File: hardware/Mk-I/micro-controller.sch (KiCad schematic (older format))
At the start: 31 parts, among them U10 STM32_SWD_Connector, U4 STM32F407VG, U8 MOLEX_microSD_47219-2001, X1 CRYSTAL

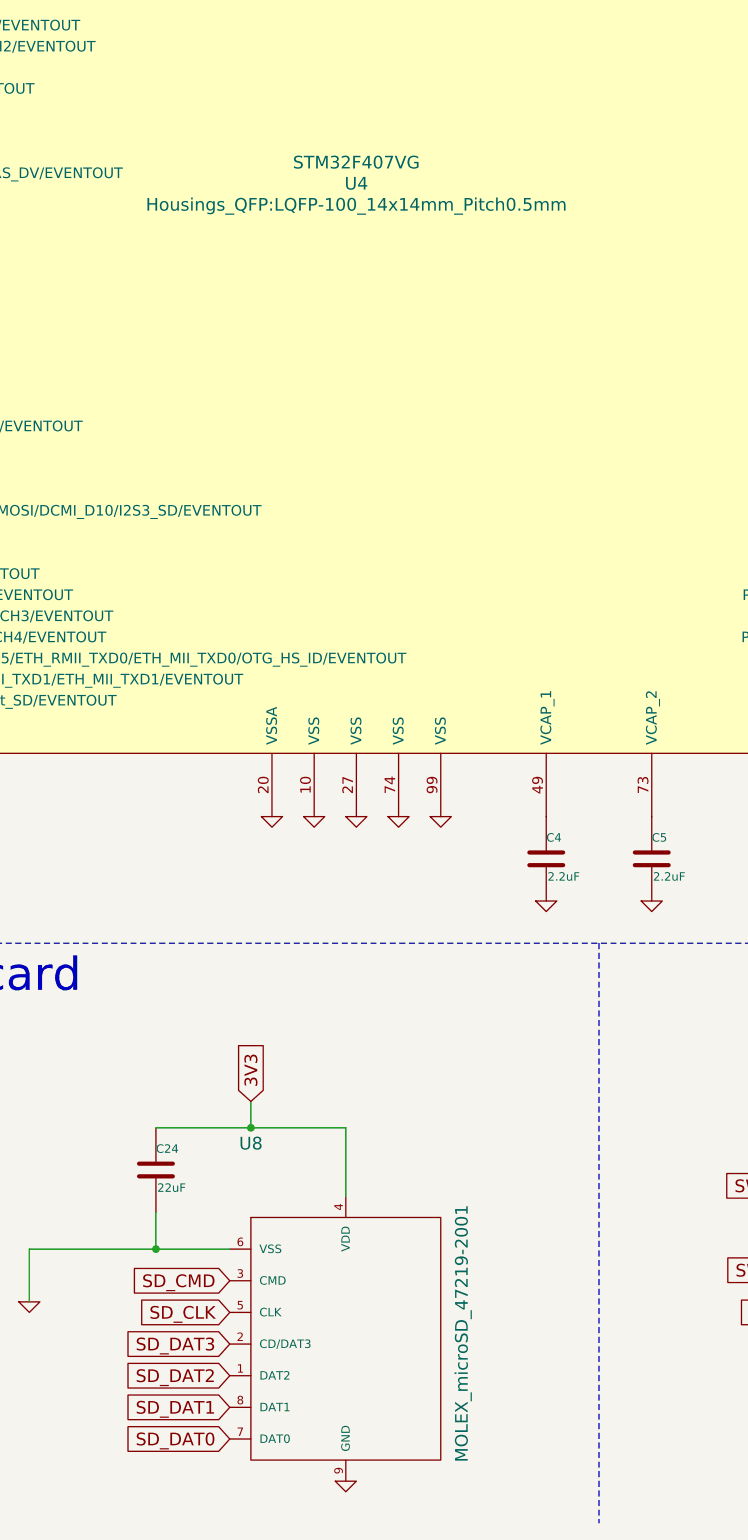
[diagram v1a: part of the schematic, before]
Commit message: HW: Update parts value
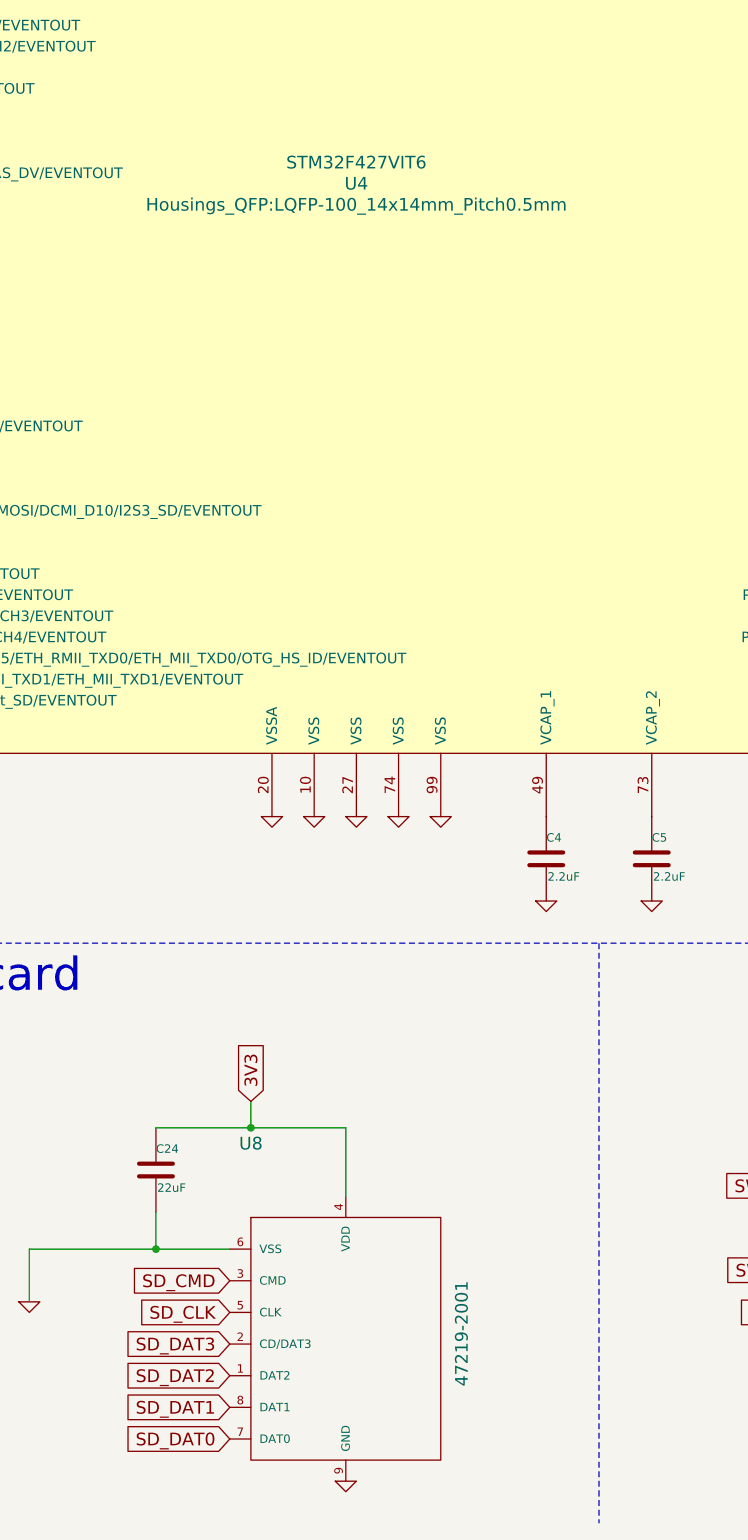
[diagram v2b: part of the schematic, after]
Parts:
- U4: value STM32F407VG -> STM32F427VIT6
- U8: value MOLEX_microSD_47219-2001 -> 47219-2001
- X1: value CRYSTAL -> AS-8.000-18
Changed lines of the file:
@@
 P 2300 3000
 F 0 "X1" H 2300 3150 60  0000 C CNN
-F 1 "CRYSTAL" H 2300 2850 60  0000 C CNN
+F 1 "AS-8.000-18" H 2300 2850 60  0000 C CNN
 F 2 "Crystals:Crystal_HC49-U_Vertical" H 2300 3000 60  0001 C CNN
 F 3 "" H 2300 3000 60  0000 C CNN
@@
 P 7850 4850
 F 0 "U4" H 7850 4850 60  0000 C CNN
-F 1 "STM32F407VG" H 7850 4950 60  0000 C CNN
+F 1 "STM32F427VIT6" H 7850 4950 60  0000 C CNN
 F 2 "Housings_QFP:LQFP-100_14x14mm_Pitch0.5mm" H 7850 4750 60  0000 C CNN
 F 3 "" H 7850 4850 60  0001 C CNN
@@
 P 7350 9400
 F 0 "U8" H 7350 9400 60  0000 C CNN
-F 1 "MOLEX_microSD_47219-2001" V 8350 8500 60  0000 C CNN
+F 1 "47219-2001" V 8350 8500 60  0000 C CNN
 F 2 "POSS:MOLEX_microSD_47219-2001" H 7350 9400 60  0001 C CNN
 F 3 "" H 7350 9400 60  0001 C CNN

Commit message: HW: Change crystal for a smd package
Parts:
- removed X1: AS-8.000-18, Crystals:Crystal_HC49-U_Vertical, symbol CRYSTAL
- added X1: ABM3B-8.000MHZ-B2-T, Crystals:Crystal_SMD_0603_4Pads, symbol Crystal_GND24
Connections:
- wire segments 46 -> 52
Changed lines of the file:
@@
 WAKEUP
-$Comp
-L CRYSTAL X1
-U 1 1 585F8666
-P 2300 3000
-F 0 "X1" H 2300 3150 60  0000 C CNN
-F 1 "AS-8.000-18" H 2300 2850 60  0000 C CNN
-F 2 "Crystals:Crystal_HC49-U_Vertical" H 2300 3000 60  0001 C CNN
-F 3 "" H 2300 3000 60  0000 C CNN
-	1    2300 3000
-	0    1    1    0
-$EndComp
 $Comp
 L C-RESCUE-wnm_mk_1 C12
@@
 Wire Wire Line
 	2600 9900 1900 9900
+$Comp
+L Crystal_GND24 X1
+U 1 1 59EB52C9
+P 2300 3000
+F 0 "X1" V 2100 3100 50  0000 L CNN
+F 1 "ABM3B-8.000MHZ-B2-T" V 1900 2350 50  0000 L CNN
+F 2 "Crystals:Crystal_SMD_0603_4Pads" H 2300 3000 50  0001 C CNN
+F 3 "" H 2300 3000 50  0001 C CNN
+	1    2300 3000
+	0    -1   -1   0
+$EndComp
+Wire Wire Line
+	2300 2700 2300 2850
+Wire Wire Line
+	2300 3150 2300 3300
+Wire Wire Line
+	2500 3000 2550 3000
+Wire Wire Line
+	2550 3000 2550 3050
+Wire Wire Line
+	2100 3000 2050 3000
+Wire Wire Line
+	2050 3000 2050 3050
+$Comp
+L GND-RESCUE-wnm_mk_1 #PWR032
+U 1 1 59EB6029
+P 2050 3050
+F 0 "#PWR032" H 2050 3050 30  0001 C CNN
+F 1 "GND" H 2050 2980 30  0001 C CNN
+F 2 "" H 2050 3050 60  0001 C CNN
+F 3 "" H 2050 3050 60  0001 C CNN
+	1    2050 3050
+	1    0    0    -1
+$EndComp
+$Comp
+L GND-RESCUE-wnm_mk_1 #PWR033
+U 1 1 59EB60D4
+P 2550 3050
+F 0 "#PWR033" H 2550 3050 30  0001 C CNN
+F 1 "GND" H 2550 2980 30  0001 C CNN
+F 2 "" H 2550 3050 60  0001 C CNN
+F 3 "" H 2550 3050 60  0001 C CNN
+	1    2550 3050
+	1    0    0    -1
+$EndComp
 $EndSCHEMATC

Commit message: HW: Major change of layout...
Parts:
- removed ext1: CONN_01X04, Socket_Strips:Socket_Strip_Straight_1x04, symbol CONN_01X04
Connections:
- net labels added: PLAY_WAKEUP
- net labels removed: B1, B11, B12, B13, B14, B15, B16, B2, B3, B4, B5, B6, B7, B8, B9, BA, BB, BC, BD, BE, FX, Play, ROW3, WAKEUP
- wire segments 52 -> 51
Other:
- moved on the sheet: R3, R4

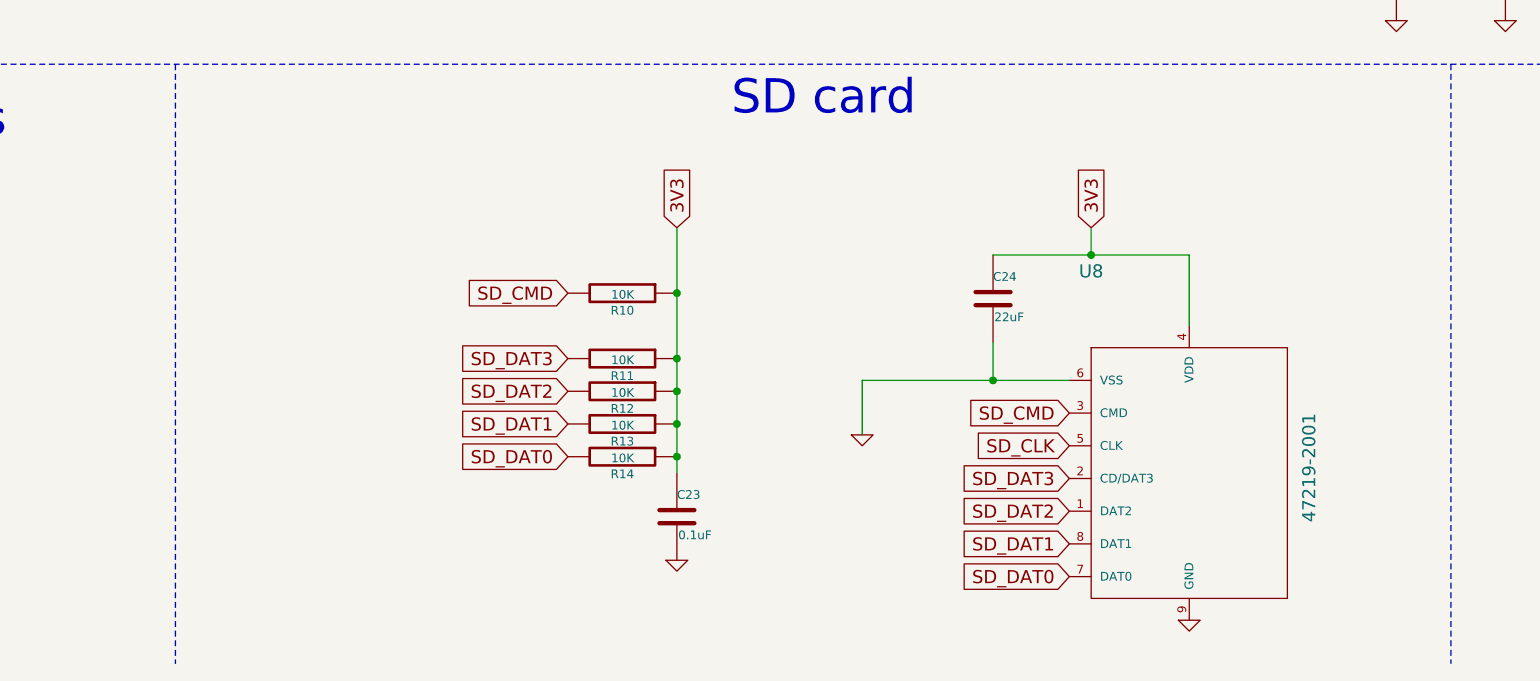
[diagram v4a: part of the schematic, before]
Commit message: HW: Change micro SD card slot
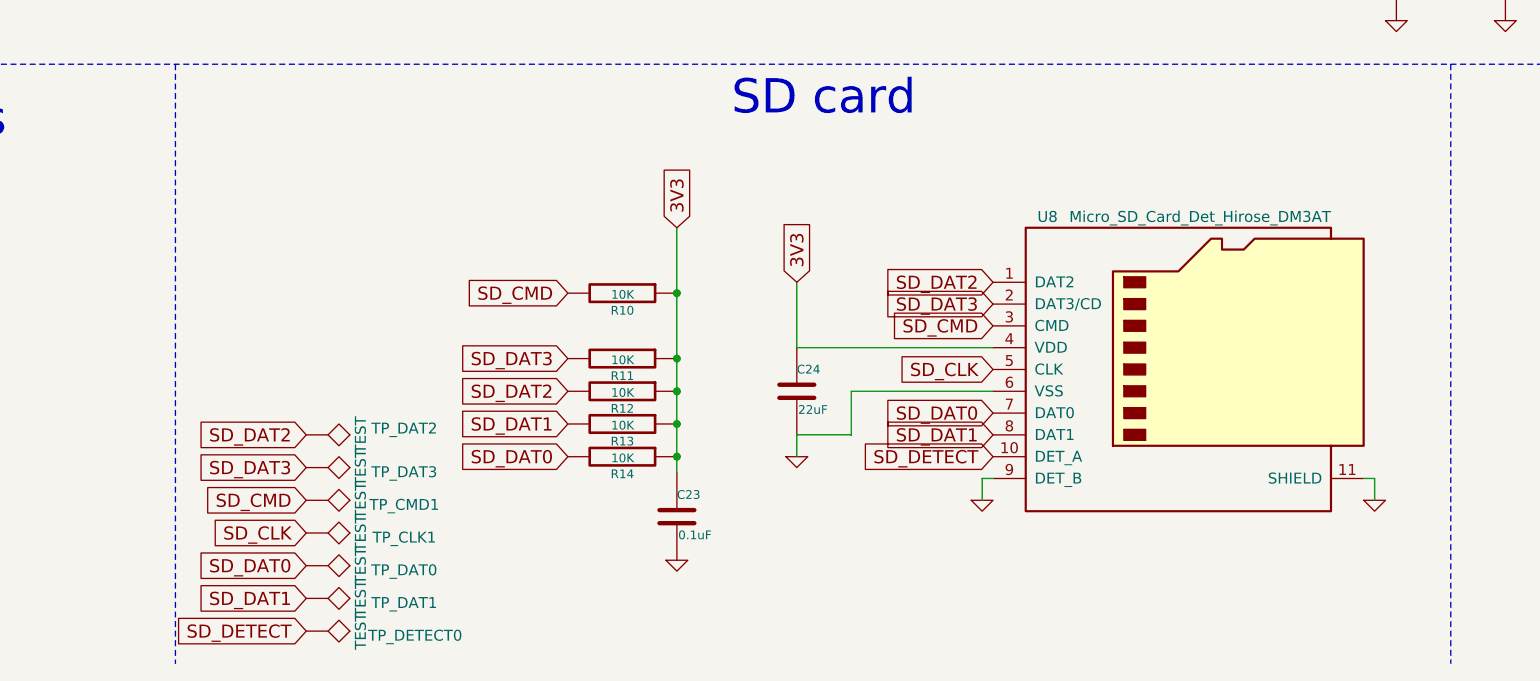
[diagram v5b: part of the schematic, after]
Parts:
- removed U8: 47219-2001, POSS:MOLEX_microSD_47219-2001, symbol MOLEX_microSD_47219-2001
- added TP_CLK1, TP_CMD1, TP_DAT0, TP_DAT1, TP_DAT2, TP_DAT3, TP_DETECT0: TEST, Measurement_Points:Measurement_Point_Round-SMD-Pad_Small, symbol TEST
- added U8: Micro_SD_Card_Det_Hirose_DM3AT, POSS:DM3D, symbol Micro_SD_Card_Det_Hirose_DM3AT
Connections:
- net 3V3: now also U8.4 (VDD)
- net GND: now also U8.11 (SHIELD), U8.6 (VSS), U8.9 (DET_B)
- net SD_CLK: now also TP_CLK1.1, U8.5 (CLK)
- net SD_CMD: now also TP_CMD1.1, U8.3 (CMD)
- net SD_DAT0: now also TP_DAT0.1, U8.7 (DAT0)
- net SD_DAT1: now also TP_DAT1.1, U8.8 (DAT1)
- net SD_DAT2: now also TP_DAT2.1, U8.1 (DAT2)
- net SD_DAT3: now also TP_DAT3.1, U8.2 (DAT3/CD)
- new net SD_DETECT: TP_DETECT0.1, U8.10 (DET_A)
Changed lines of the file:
@@
 Title "Wee Noise Maker - Mk-I"
 Date ""
-Rev "C"
+Rev "D"
 Comp "Fabien Chouteau"
 Comment1 ""
@@
 Text GLabel 12850 3200 2    60   Input ~ 0
 COL5
-$Comp
-L MOLEX_microSD_47219-2001 U8
-U 1 1 58639490
-P 7350 9400
-F 0 "U8" H 7350 9400 60  0000 C CNN
-F 1 "47219-2001" V 8350 8500 60  0000 C CNN
-F 2 "POSS:MOLEX_microSD_47219-2001" H 7350 9400 60  0001 C CNN
-F 3 "" H 7350 9400 60  0001 C CNN
-	1    7350 9400
-	1    0    0    -1
-$EndComp
-$Comp
-L GND-RESCUE-wnm_mk_1 #PWR027
-U 1 1 586394FE
-P 7800 11000
-AR Path="/586394FE" Ref="#PWR027"  Part="1"
-AR Path="/585DBE08/586394FE" Ref="#PWR021"  Part="1"
-F 0 "#PWR021" H 7800 11000 30  0001 C CNN
-F 1 "GND" H 7800 10930 30  0001 C CNN
-F 2 "" H 7800 11000 60  0001 C CNN
-F 3 "" H 7800 11000 60  0001 C CNN
-	1    7800 11000
-	1    0    0    -1
-$EndComp
 Text GLabel 4950 9950 0    60   Input ~ 0
 SD_DAT2
@@
 Text GLabel 4950 10100 0    60   Input ~ 0
 SD_DAT1
-Text GLabel 7350 9200 1    60   Input ~ 0
-3V3
 Text GLabel 12850 7000 2    60   Input ~ 0
 SD_DAT3
@@
 Text GLabel 12850 4300 2    60   Input ~ 0
 SD_CMD
-$Comp
-L GND-RESCUE-wnm_mk_1 #PWR028
-U 1 1 58631320
-P 6300 10150
-AR Path="/58631320" Ref="#PWR028"  Part="1"
-AR Path="/585DBE08/58631320" Ref="#PWR022"  Part="1"
-F 0 "#PWR022" H 6300 10150 30  0001 C CNN
-F 1 "GND" H 6300 10080 30  0001 C CNN
-F 2 "" H 6300 10150 60  0001 C CNN
-F 3 "" H 6300 10150 60  0001 C CNN
-	1    6300 10150
-	1    0    0    -1
-$EndComp
 Text GLabel 2850 5900 0    60   Input ~ 0
 COL4
@@
 Text GLabel 5450 9200 1    60   Input ~ 0
 3V3
-Text GLabel 7250 10500 0    60   Input ~ 0
+Text GLabel 6900 9450 0    60   Input ~ 0
 SD_DAT2
-Text GLabel 7250 10350 0    60   Input ~ 0
+Text GLabel 6900 9550 0    60   Input ~ 0
 SD_DAT3
-Text GLabel 7250 10050 0    60   Input ~ 0
+Text GLabel 6900 9650 0    60   Input ~ 0
 SD_CMD
-Text GLabel 7250 10800 0    60   Input ~ 0
+Text GLabel 6900 10050 0    60   Input ~ 0
 SD_DAT0
-Text GLabel 7250 10650 0    60   Input ~ 0
+Text GLabel 6900 10150 0    60   Input ~ 0
 SD_DAT1
-Text GLabel 7250 10200 0    60   Input ~ 0
+Text GLabel 6900 9850 0    60   Input ~ 0
 SD_CLK
 $Comp
@@
 P 5450 10725
 AR Path="/58640311" Ref="#PWR029"  Part="1"
-AR Path="/585DBE08/58640311" Ref="#PWR023"  Part="1"
-F 0 "#PWR023" H 5450 10725 30  0001 C CNN
+AR Path="/585DBE08/58640311" Ref="#PWR021"  Part="1"
+F 0 "#PWR021" H 5450 10725 30  0001 C CNN
 F 1 "GND" H 5450 10655 30  0001 C CNN
 F 2 "" H 5450 10725 60  0001 C CNN
 F 3 "" H 5450 10725 60  0001 C CNN
 	1    5450 10725
-	1    0    0    -1
-$EndComp
-$Comp
-L C-RESCUE-wnm_mk_1 C24
-U 1 1 58640860
-P 6900 9525
-AR Path="/58640860" Ref="C24"  Part="1"
-AR Path="/585DBE08/58640860" Ref="C24"  Part="1"
-F 0 "C24" H 6900 9625 40  0000 L CNN
-F 1 "22uF" H 6906 9440 40  0000 L CNN
-F 2 "Capacitors_SMD:C_0805" H 6938 9375 30  0001 C CNN
-F 3 "" H 6900 9525 60  0000 C CNN
-	1    6900 9525
 	1    0    0    -1
 $EndComp
@@
 P 9900 9850
 AR Path="/586649ED" Ref="#PWR030"  Part="1"
-AR Path="/585DBE08/586649ED" Ref="#PWR024"  Part="1"
-F 0 "#PWR024" H 9900 9850 30  0001 C CNN
+AR Path="/585DBE08/586649ED" Ref="#PWR022"  Part="1"
+F 0 "#PWR022" H 9900 9850 30  0001 C CNN
 F 1 "GND" H 9900 9780 30  0001 C CNN
 F 2 "" H 9900 9850 60  0001 C CNN
@@
 	1700 9450 1700 9600
 Wire Wire Line
-	7250 9900 6300 9900
-Wire Wire Line
-	6300 9900 6300 10150
-Wire Wire Line
 	5450 9200 5450 10325
 Connection ~ 5450 9950
@@
 Connection ~ 5450 9500
 Connection ~ 5450 10250
-Wire Wire Line
-	6900 9725 6900 9900
-Connection ~ 6900 9900
-Wire Wire Line
-	7800 9650 7800 9325
-Wire Wire Line
-	7800 9325 6900 9325
-Wire Wire Line
-	7350 9200 7350 9325
-Connection ~ 7350 9325
 Wire Wire Line
 	9900 9850 9900 9800
@@
 	2050 3000 2050 3050
 $Comp
-L GND-RESCUE-wnm_mk_1 #PWR026
+L GND-RESCUE-wnm_mk_1 #PWR023
 U 1 1 59EB6029
 P 2050 3050
-F 0 "#PWR026" H 2050 3050 30  0001 C CNN
+F 0 "#PWR023" H 2050 3050 30  0001 C CNN
 F 1 "GND" H 2050 2980 30  0001 C CNN
 F 2 "" H 2050 3050 60  0001 C CNN
@@
 $EndComp
 $Comp
-L GND-RESCUE-wnm_mk_1 #PWR027
+L GND-RESCUE-wnm_mk_1 #PWR024
 U 1 1 59EB60D4
 P 2550 3050
-F 0 "#PWR027" H 2550 3050 30  0001 C CNN
+F 0 "#PWR024" H 2550 3050 30  0001 C CNN
 F 1 "GND" H 2550 2980 30  0001 C CNN
 F 2 "" H 2550 3050 60  0001 C CNN
@@
 	1    0    0    -1
 $EndComp
+$Comp
+L Micro_SD_Card_Det_Hirose_DM3AT U8
+U 1 1 59EDB226
+P 7800 9850
+F 0 "U8" H 7150 10550 50  0000 C CNN
+F 1 "Micro_SD_Card_Det_Hirose_DM3AT" H 8450 10550 50  0000 R CNN
+F 2 "POSS:DM3D" H 9850 10550 50  0001 C CNN
+F 3 "" H 7800 9950 50  0001 C CNN
+	1    7800 9850
+	1    0    0    -1
+$EndComp
+Text GLabel 6000 9450 1    60   Input ~ 0
+3V3
+$Comp
+L GND-RESCUE-wnm_mk_1 #PWR025
+U 1 1 59EDEF62
+P 6000 10250
+F 0 "#PWR025" H 6000 10250 30  0001 C CNN
+F 1 "GND" H 6000 10180 30  0001 C CNN
+F 2 "" H 6000 10250 60  0001 C CNN
+F 3 "" H 6000 10250 60  0001 C CNN
+	1    6000 10250
+	1    0    0    -1
+$EndComp
+$Comp
+L C-RESCUE-wnm_mk_1 C24
+U 1 1 59EDEF68
+P 6000 9950
+F 0 "C24" H 6000 10050 40  0000 L CNN
+F 1 "22uF" H 6006 9865 40  0000 L CNN
+F 2 "Capacitors_SMD:C_0805" H 6038 9800 30  0001 C CNN
+F 3 "" H 6000 9950 60  0000 C CNN
+	1    6000 9950
+	1    0    0    -1
+$EndComp
+Wire Wire Line
+	6900 9750 6000 9750
+Wire Wire Line
+	6000 9750 6000 9450
+Wire Wire Line
+	6900 9950 6250 9950
+Wire Wire Line
+	6250 9950 6250 10150
+Wire Wire Line
+	6250 10150 6000 10150
+Wire Wire Line
+	6000 10150 6000 10250
+$Comp
+L GND-RESCUE-wnm_mk_1 #PWR026
+U 1 1 59EE3B60
+P 8650 10450
+F 0 "#PWR026" H 8650 10450 30  0001 C CNN
+F 1 "GND" H 8650 10380 30  0001 C CNN
+F 2 "" H 8650 10450 60  0001 C CNN
+F 3 "" H 8650 10450 60  0001 C CNN
+	1    8650 10450
+	1    0    0    -1
+$EndComp
+Wire Wire Line
+	8600 10350 8650 10350
+Wire Wire Line
+	8650 10350 8650 10450
+$Comp
+L GND-RESCUE-wnm_mk_1 #PWR027
+U 1 1 59EE3EE8
+P 6850 10450
+F 0 "#PWR027" H 6850 10450 30  0001 C CNN
+F 1 "GND" H 6850 10380 30  0001 C CNN
+F 2 "" H 6850 10450 60  0001 C CNN
+F 3 "" H 6850 10450 60  0001 C CNN
+	1    6850 10450
+	1    0    0    -1
+$EndComp
+Wire Wire Line
+	6900 10350 6850 10350
+Wire Wire Line
+	6850 10350 6850 10450
+Text GLabel 6900 10250 0    60   Input ~ 0
+SD_DETECT
+Text GLabel 3750 10150 0    60   Input ~ 0
+SD_DAT2
+Text GLabel 3750 10300 0    60   Input ~ 0
+SD_DAT3
+Text GLabel 3750 10450 0    60   Input ~ 0
+SD_CMD
+Text GLabel 3750 10750 0    60   Input ~ 0
+SD_DAT0
+Text GLabel 3750 10900 0    60   Input ~ 0
+SD_DAT1
+Text GLabel 3750 10600 0    60   Input ~ 0
+SD_CLK
+Text GLabel 3750 11050 0    60   Input ~ 0
+SD_DETECT
+$Comp
+L TEST TP_DAT2
+U 1 1 59EE5E47
+P 3750 10150
+F 0 "TP_DAT2" V 3750 10600 50  0000 C BNN
+F 1 "TEST" H 3750 10400 50  0000 C CNN
+F 2 "Measurement_Points:Measurement_Point_Round-SMD-Pad_Small" H 3750 10150 50  0001 C CNN
+F 3 "" H 3750 10150 50  0001 C CNN
+	1    3750 10150
+	0    1    1    0
+$EndComp
+$Comp
+L TEST TP_DAT3
+U 1 1 59EE61E0
+P 3750 10300
+F 0 "TP_DAT3" V 3800 10750 50  0000 C BNN
+F 1 "TEST" H 3750 10550 50  0000 C CNN
+F 2 "Measurement_Points:Measurement_Point_Round-SMD-Pad_Small" H 3750 10300 50  0001 C CNN
+F 3 "" H 3750 10300 50  0001 C CNN
+	1    3750 10300
+	0    1    1    0
+$EndComp
+$Comp
+L TEST TP_CMD1
+U 1 1 59EE6254
+P 3750 10450
+F 0 "TP_CMD1" V 3800 10900 50  0000 C BNN
+F 1 "TEST" H 3750 10700 50  0000 C CNN
+F 2 "Measurement_Points:Measurement_Point_Round-SMD-Pad_Small" H 3750 10450 50  0001 C CNN
+F 3 "" H 3750 10450 50  0001 C CNN
+	1    3750 10450
+	0    1    1    0
+$EndComp
+$Comp
+L TEST TP_CLK1
+U 1 1 59EE62C7
+P 3750 10600
+F 0 "TP_CLK1" V 3800 11050 50  0000 C BNN
+F 1 "TEST" H 3750 10850 50  0000 C CNN
+F 2 "Measurement_Points:Measurement_Point_Round-SMD-Pad_Small" H 3750 10600 50  0001 C CNN
+F 3 "" H 3750 10600 50  0001 C CNN
+	1    3750 10600
+	0    1    1    0
+$EndComp
+$Comp
+L TEST TP_DAT0
+U 1 1 59EE662D
+P 3750 10750
+F 0 "TP_DAT0" V 3800 11200 50  0000 C BNN
+F 1 "TEST" H 3750 11000 50  0000 C CNN
+F 2 "Measurement_Points:Measurement_Point_Round-SMD-Pad_Small" H 3750 10750 50  0001 C CNN
+F 3 "" H 3750 10750 50  0001 C CNN
+	1    3750 10750
+	0    1    1    0
+$EndComp
+$Comp
+L TEST TP_DAT1
+U 1 1 59EE66AA
+P 3750 10900
+F 0 "TP_DAT1" V 3800 11350 50  0000 C BNN
+F 1 "TEST" H 3750 11150 50  0000 C CNN
+F 2 "Measurement_Points:Measurement_Point_Round-SMD-Pad_Small" H 3750 10900 50  0001 C CNN
+F 3 "" H 3750 10900 50  0001 C CNN
+	1    3750 10900
+	0    1    1    0
+$EndComp
+$Comp
+L TEST TP_DETECT0
+U 1 1 59EE6726
+P 3750 11050
+F 0 "TP_DETECT0" V 3800 11550 50  0000 C BNN
+F 1 "TEST" H 3750 11300 50  0000 C CNN
+F 2 "Measurement_Points:Measurement_Point_Round-SMD-Pad_Small" H 3750 11050 50  0001 C CNN
+F 3 "" H 3750 11050 50  0001 C CNN
+	1    3750 11050
+	0    1    1    0
+$EndComp
 $EndSCHEMATC
